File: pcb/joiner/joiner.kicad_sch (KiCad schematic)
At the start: 1 part, among them U1 ESP32-S3-WROOM-1

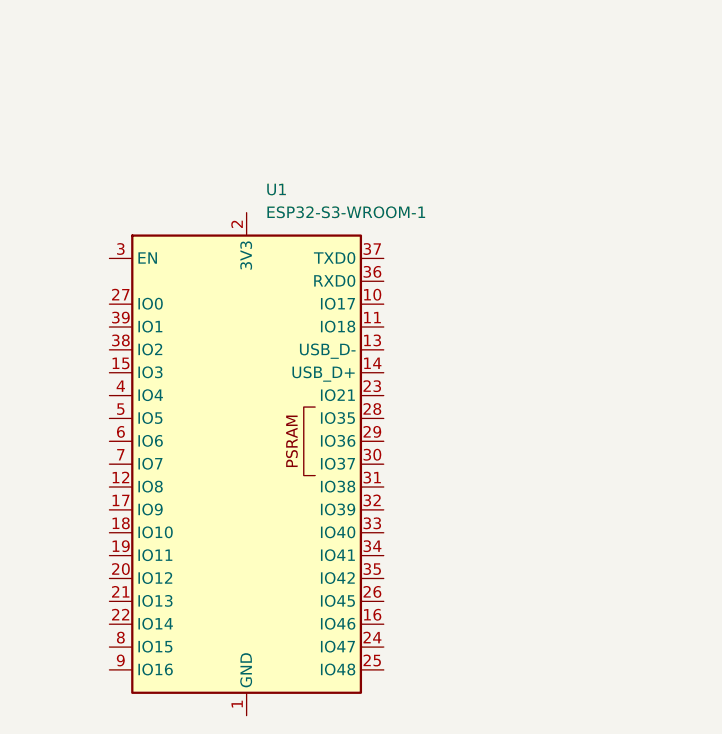
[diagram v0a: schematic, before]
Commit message: arduino case, kicad basic setup
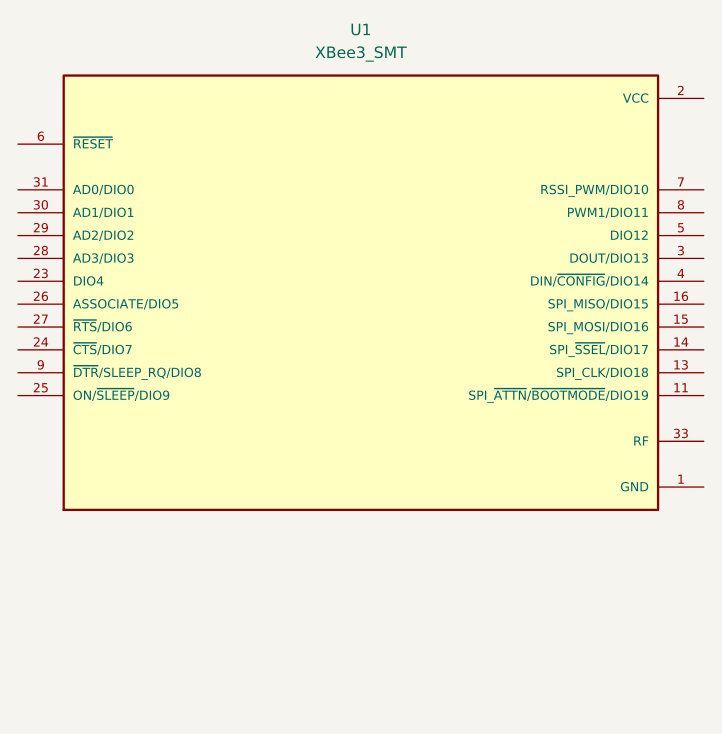
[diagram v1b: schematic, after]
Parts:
- removed U1: ESP32-S3-WROOM-1, RF_Module:ESP32-S3-WROOM-1U, symbol RF_Module:ESP32-S3-WROOM-1
- added U1: XBee3_SMT, XBee3:XBee3_SMT, symbol XBee3_SMT:XBee3_SMT
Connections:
- new net GND: U1.1 (GND), U1.10 (GND), U1.12 (GND), U1.21 (GND), U1.32 (GND), U1.34 (GND)
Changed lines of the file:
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@@
 (kicad_sch
-	(version 20250114)
+	(version 20260306)
 	(generator "eeschema")
-	(generator_version "9.0")
+	(generator_version "10.0")
 	(paper "A4")
 	(symbol
-		(lib_id "RF_Module:ESP32-S3-WROOM-1")
-		(at 147.32 93.98 0)
+		(lib_id "XBee3_SMT:XBee3_SMT")
+		(at 160.02 76.2 0)
 		(unit 1)
+		(body_style 1)
 		(exclude_from_sim no)
 		(in_bom yes)
 		(on_board yes)
+		(in_pos_files yes)
 		(dnp no)
 		(fields_autoplaced yes)
 		(property "Reference" "U1"
-			(at 149.4633 63.5 0)
-			(effects
-				(font
-					(size 1.27 1.27)
-				)
-				(justify left)
-			)
-		)
-		(property "Value" "ESP32-S3-WROOM-1"
-			(at 149.4633 66.04 0)
-			(effects
-				(font
-					(size 1.27 1.27)
-				)
-				(justify left)
-			)
-		)
-		(property "Footprint" "RF_Module:ESP32-S3-WROOM-1U"
-			(at 147.32 91.44 0)
-			(effects
-				(font
-					(size 1.27 1.27)
-				)
-				(hide yes)
-			)
-		)
-		(property "Datasheet" "https://www.espressif.com/sites/default/files/documentation/esp32-s3-wroom-1_wroom-1u_datasheet_en.pdf"
-			(at 147.32 93.98 0)
-			(effects
-				(font
-					(size 1.27 1.27)
-				)
-				(hide yes)
-			)
-		)
-		(property "Description" "RF Module, ESP32-S3 SoC, Wi-Fi 802.11b/g/n, Bluetooth, BLE, 32-bit, 3.3V, onboard antenna, SMD"
-			(at 147.32 93.98 0)
-			(effects
-				(font
-					(size 1.27 1.27)
-				)
-				(hide yes)
-			)
+			(at 160.02 45.72 0)
+			(show_name no)
+			(do_not_autoplace no)
+			(effects
+				(font
+					(size 1.27 1.27)
+				)
+			)
+		)
+		(property "Value" "XBee3_SMT"
+			(at 160.02 48.26 0)
+			(show_name no)
+			(do_not_autoplace no)
+			(effects
+				(font
+					(size 1.27 1.27)
+				)
+			)
+		)
+		(property "Footprint" "XBee3:XBee3_SMT"
+			(at 160.02 76.2 0)
+			(hide yes)
+			(show_name no)
+			(do_not_autoplace no)
+			(effects
+				(font
+					(size 1.27 1.27)
+				)
+				(justify bottom)
+			)
+		)
+		(property "Datasheet" ""
+			(at 160.02 76.2 0)
+			(hide yes)
+			(show_name no)
+			(do_not_autoplace no)
+			(effects
+				(font
+					(size 1.27 1.27)
+				)
+			)
+		)
+		(property "Description" "802.15.4 Zigbee® Transceiver Module 2.4GHz Antenna Not Included, U.FL Surface Mount"
+			(at 160.02 76.2 0)
+			(hide yes)
+			(show_name no)
+			(do_not_autoplace no)
+			(effects
+				(font
+					(size 1.27 1.27)
+				)
+				(justify bottom)
+			)
+		)
+		(property "MF" "Digi International"
+			(at 160.02 76.2 0)
+			(hide yes)
+			(show_name no)
+			(do_not_autoplace no)
+			(effects
+				(font
+					(size 1.27 1.27)
+				)
+				(justify bottom)
+			)
+		)
+		(property "Package" "SMD-34 Digi International"
+			(at 160.02 76.2 0)
+			(hide yes)
+			(show_name no)
+			(do_not_autoplace no)
+			(effects
+				(font
+					(size 1.27 1.27)
+				)
+				(justify bottom)
+			)
+		)
+		(property "Price" "None"
+			(at 160.02 76.2 0)
+			(hide yes)
+			(show_name no)
+			(do_not_autoplace no)
+			(effects
+				(font
+					(size 1.27 1.27)
+				)
+				(justify bottom)
+			)
+		)
+		(property "Check_prices" "https://www.snapeda.com/parts/XB3-24Z8UM-J/Digi+International/view-part/?ref=eda"
+			(at 160.02 76.2 0)
+			(hide yes)
+			(show_name no)
+			(do_not_autoplace no)
+			(effects
+				(font
+					(size 1.27 1.27)
+				)
+				(justify bottom)
+			)
+		)
+		(property "STANDARD" "Manufacturer Recommendations"
+			(at 160.02 76.2 0)
+			(hide yes)
+			(show_name no)
+			(do_not_autoplace no)
+			(effects
+				(font
+					(size 1.27 1.27)
+				)
+				(justify bottom)
+			)
+		)
+		(property "SnapEDA_Link" "https://www.snapeda.com/parts/XB3-24Z8UM-J/Digi+International/view-part/?ref=snap"
+			(at 160.02 76.2 0)
+			(hide yes)
+			(show_name no)
+			(do_not_autoplace no)
+			(effects
+				(font
+					(size 1.27 1.27)
+				)
+				(justify bottom)
+			)
+		)
+		(property "MP" "XB3-24Z8UM-J"
+			(at 160.02 76.2 0)
+			(hide yes)
+			(show_name no)
+			(do_not_autoplace no)
+			(effects
+				(font
+					(size 1.27 1.27)
+				)
+				(justify bottom)
+			)
+		)
+		(property "Availability" "In Stock"
+			(at 160.02 76.2 0)
+			(hide yes)
+			(show_name no)
+			(do_not_autoplace no)
+			(effects
+				(font
+					(size 1.27 1.27)
+				)
+				(justify bottom)
+			)
+		)
+		(property "MANUFACTURER" "DIGI"
+			(at 160.02 76.2 0)
+			(hide yes)
+			(show_name no)
+			(do_not_autoplace no)
+			(effects
+				(font
+					(size 1.27 1.27)
+				)
+				(justify bottom)
+			)
+		)
+		(pin "24"
+		)
+		(pin "7"
 		)
 		(pin "14"
 		)
+		(pin "11"
+		)
+		(pin "8"
+		)
+		(pin "13"
+		)
 		(pin "27"
 		)
-		(pin "37"
-		)
-		(pin "18"
+		(pin "10"
+		)
+		(pin "32"
+		)
+		(pin "29"
+		)
+		(pin "33"
+		)
+		(pin "16"
+		)
+		(pin "25"
+		)
+		(pin "30"
+		)
+		(pin "31"
+		)
+		(pin "34"
+		)
+		(pin "21"
 		)
 		(pin "26"
 		)
-		(pin "25"
-		)
-		(pin "10"
+		(pin "9"
 		)
 		(pin "6"
 		)
-		(pin "16"
+		(pin "5"
+		)
+		(pin "4"
 		)
 		(pin "3"
 		)
-		(pin "11"
-		)
-		(pin "19"
-		)
-		(pin "24"
-		)
-		(pin "41"
-		)
-		(pin "33"
-		)
-		(pin "20"
-		)
-		(pin "36"
-		)
-		(pin "30"
+		(pin "2"
+		)
+		(pin "1"
+		)
+		(pin "28"
+		)
+		(pin "15"
 		)
 		(pin "23"
 		)
-		(pin "8"
-		)
-		(pin "40"
-		)
-		(pin "29"
-		)
-		(pin "28"
-		)
-		(pin "39"
-		)
-		(pin "35"
-		)
-		(pin "2"
-		)
-		(pin "1"
-		)
-		(pin "34"
-		)
-		(pin "38"
-		)
-		(pin "4"
-		)
-		(pin "22"
-		)
-		(pin "15"
-		)
-		(pin "5"
-		)
-		(pin "13"
-		)
-		(pin "7"
-		)
-		(pin "31"
-		)
 		(pin "12"
 		)
-		(pin "17"
-		)
-		(pin "32"
-		)
-		(pin "9"
-		)
-		(pin "21"
-		)
 		(instances
-			(project ""
+			(project "joiner"
 				(path "/a031f6db-95e5-4399-b2a9-8a481c990ac3"
 					(reference "U1")
